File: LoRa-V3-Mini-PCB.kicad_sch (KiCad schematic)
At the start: 23 parts, among them Q1 SI2367DS-T1-GE3, SW1 434331045822, SW2 434331045816, U1 114993121, U2 BR24G1MFVT, U3 SHT40, U4 TSL25911

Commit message: finishing touch to layout
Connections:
- net GND: now also U2.1 (A0)
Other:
- moved on the sheet: C1, C10, C2, U3, U4

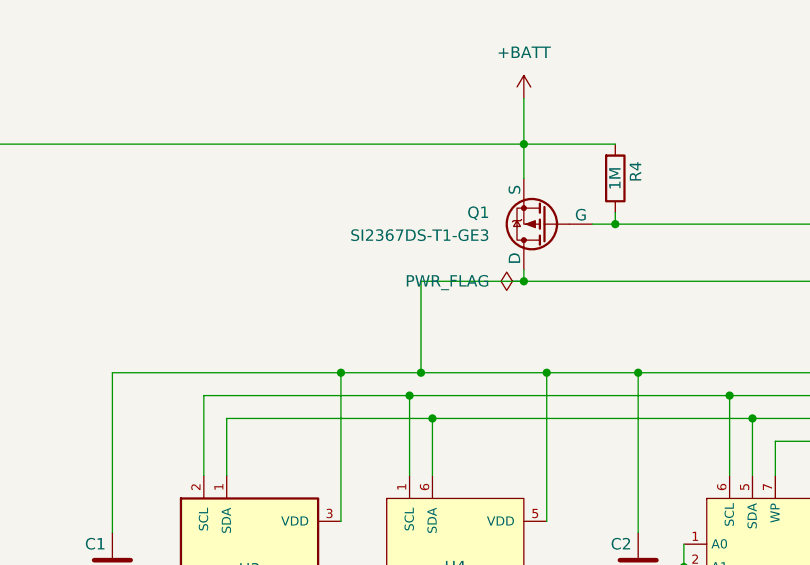
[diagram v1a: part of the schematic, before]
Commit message: change caps to 0805
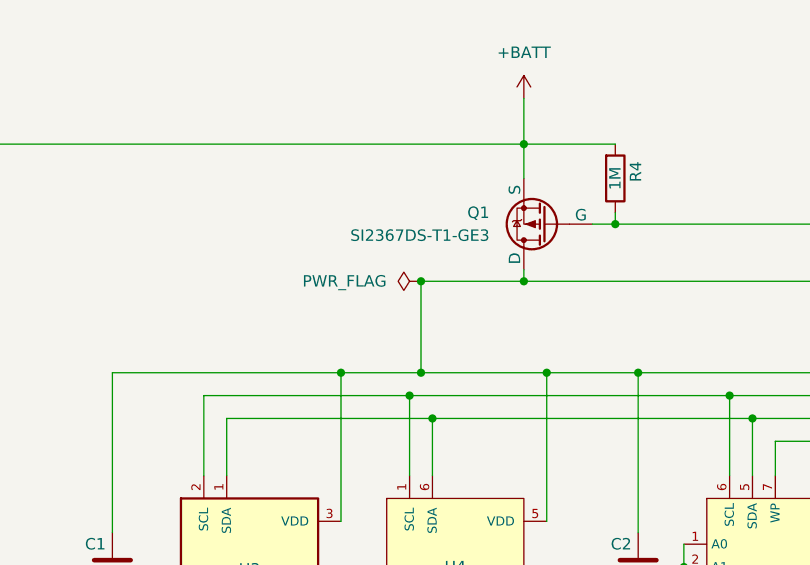
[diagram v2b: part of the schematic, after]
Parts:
- C10, C11: footprint 1projectLibrary:C_0603_nominal -> 1GlobalFootprintsLibrary:C_0805
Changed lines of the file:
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@@
 	)
 	(junction
+		(at 76.2 66.04)
+		(diameter 0)
+		(color 0 0 0 0)
+	)
+	(junction
 		(at 69.85 111.76)
 		(diameter 0)
@@
 	(wire
 		(pts
-			(xy 76.2 66.04) (xy 87.63 66.04)
-		)
-		(stroke
-			(width 0)
-			(type default)
-		)
-	)
-	(wire
-		(pts
 			(xy 241.3 52.07) (xy 241.3 88.9)
 		)
@@
 	(wire
 		(pts
+			(xy 76.2 66.04) (xy 87.63 66.04)
+		)
+		(stroke
+			(width 0)
+			(type default)
+		)
+	)
+	(wire
+		(pts
 			(xy 231.14 57.15) (xy 231.14 48.26)
 		)
@@
 	(symbol
 		(lib_id "power:PWR_FLAG")
-		(at 87.63 66.04 90)
+		(at 76.2 66.04 90)
 		(unit 1)
 		(exclude_from_sim no)
@@
 		(fields_autoplaced yes)
 		(property "Reference" "#FLG01"
-			(at 85.725 66.04 0)
+			(at 74.295 66.04 0)
 			(effects
 				(font
@@
 		)
 		(property "Value" "PWR_FLAG"
-			(at 83.82 66.0399 90)
+			(at 72.39 66.0399 90)
 			(effects
 				(font
@@
 		)
 		(property "Footprint" ""
-			(at 87.63 66.04 0)
+			(at 76.2 66.04 0)
 			(effects
 				(font
@@
 		)
 		(property "Datasheet" "~"
-			(at 87.63 66.04 0)
+			(at 76.2 66.04 0)
 			(effects
 				(font
@@
 		)
 		(property "Description" "Special symbol for telling ERC where power comes from"
-			(at 87.63 66.04 0)
+			(at 76.2 66.04 0)
 			(effects
 				(font
@@
 			)
 		)
-		(property "Footprint" "1projectLibrary:C_0603_nominal"
+		(property "Footprint" "1GlobalFootprintsLibrary:C_0805"
 			(at 25.7048 101.6 0)
 			(effects
@@
 			)
 		)
-		(property "Footprint" "1projectLibrary:C_0603_nominal"
+		(property "Footprint" "1GlobalFootprintsLibrary:C_0805"
 			(at 253.6952 62.23 0)
 			(effects

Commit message: fix BOM
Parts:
- ANT1: value ANT-868-CHP-T -> Chip Antenna; digikeyPartNumber ANT-868-CHP-TCT-ND -> (none); mouserPartNumber 712-ANT-868-CHP-T -> (none)
- BH1: value 108 -> Battery Holder; digikeyPartNumber 36-108-ND -> (none); mouserPartNumber 534-108 -> (none)
- C1, C2, C3, C5: value CGA3E2X7R1E104K080AA -> 100nF; digikeyPartNumber 445-5667-1-ND -> (none); mouserPartNumber 810-CGA3E2X7R1E104K -> (none)
- C10, C11: value C1608X7S1A475K080AC -> 4.7uF; footprint 1GlobalFootprintsLibrary:C_0805 -> 1projectLibrary:C_0805; GPN GPC0603475-10-X7S -> NA; digikeyPartNumber 445-14258-1-ND -> (none); manufacturerName TDK -> Samsung; manufacturerPartNumber C1608X7S1A475K080AC -> CL21B475KPFNFNE; mouserPartNumber 810-C1608X7S1A475KAC -> (none); octopartUrl https://octopart.com/c1608x7s1a475k080ac-tdk-28168672?r=sp -> https://octopart.com/cl21b475kpfnfne-samsung+electro-mechan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
- CONN5, F1, F2, F3: digikeyPartNumber NA -> (none); mouserPartNumber NA -> (none)
- Q1: value SI2367DS-T1-GE3 -> NA; digikeyPartNumber SI2367DS-T1-GE3TR-ND -> (none); mouserPartNumber 781-SI2367DS-GE3 -> (none)
- R1, R2, R3: value CR0603-FX-4701ELF -> 4K7; GPN GPR06034K7 -> 4K7; digikeyPartNumber CR0603-FX-4701ELFCT-ND -> (none); manufacturerName Bourns -> YAGEO; mouserPartNumber 652-CR0402FX-4701GLF -> (none)
- R4: value CR0603-FX-1004ELF -> 330K; GPN GPR06031M -> 330K; digikeyPartNumber CR0603-FX-1004ELFCT-ND -> (none); manufacturerName Bourns -> YAGEO; manufacturerPartNumber CR0603-FX-1004ELF -> AC0603JR-07330KL; mouserPartNumber 652-CR0603FX-1004ELF -> (none); octopartUrl https://octopart.com/cr0603-fx-1004elf-bourns-3899435?r=sp -> https://octopart.com/ac0603jr-07330kl-yageo-30510863
- SW1: value 434331045822 -> Application Button; digikeyPartNumber 732-7055-1-ND -> (none); manufacturerName Wurth Electronics -> Wurth Elektronik; manufacturerPartNumber 434133025816 -> 434351045816; mouserPartNumber 710-434331045822 -> (none); octopartUrl https://octopart.com/434331045822-wurth+elektronik-22866031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 -> https://octopart.com/434351045816-wurth+elektronik-22866030
- SW2: value 434331045816 -> MCU Reset; manufacturerName Wurth Electronics -> Wurth Elektronik; manufacturerPartNumber 434331045816 -> 434133025816; octopartUrl (none) -> https://octopart.com/434133025816-wurth+elektronik-99472342
- U1: value 114993121 -> Lora-E5; digikeyPartNumber 1597-114993121-ND -> (none); mouserPartNumber 713-114993121 -> (none)
- U2: digikeyPartNumber 846-BR24G1MFVT-5AE2CT-ND -> (none); mouserPartNumber 755-BR24G1MFVT-5AE2 -> (none)
- U3: digikeyPartNumber 1649-SHT40-BD1B-R2CT-ND -> (none); mouserPartNumber 403-SHT40-AD1F-R2 -> (none)
- U4: digikeyPartNumber TSL25911FNCT-ND -> (none); mouserPartNumber 985-TSL25911FN -> (none)
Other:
- moved on the sheet: C10
